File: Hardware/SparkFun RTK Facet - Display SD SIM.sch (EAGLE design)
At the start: 31 parts, among them J1 FPC_12_0.5MM2, J16 microSD, J17 NANO_SIM, J2 FPC_12_0.5MM2, U13 LIS2DH12

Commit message: Update PROD ID on 12 pin connector. Add gerbers for v10.
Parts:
- J1, J2: value FPC_12_0.5MM2 -> FPC_12_0.5MM_BACKFLIP; device RTK Facet:FPC_12_0.5MM2 -> RTK Facet:FPC_12_0.5MM_BACKFLIP
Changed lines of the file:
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@@
 <part name="SUPPLY3" library="SparkFun-PowerSymbols" deviceset="3.3V" device=""/>
 <part name="GND2" library="SparkFun-PowerSymbols" deviceset="GND" device=""/>
-<part name="J1" library="RTK Facet" deviceset="FPC_12_0.5MM" device="2" value="FPC_12_0.5MM2"/>
+<part name="J1" library="RTK Facet" deviceset="FPC_12_0.5MM" device="_BACKFLIP" value="FPC_12_0.5MM_BACKFLIP"/>
 <part name="U13" library="SparkFun-Sensors" deviceset="LIS2DH12" device=""/>
 <part name="GND4" library="SparkFun-PowerSymbols" deviceset="GND" device=""/>
@@
 <part name="J17" library="ublox" deviceset="NANO_SIM" device="WURTH" value="NANO_SIM"/>
 <part name="GND5" library="SparkFun-PowerSymbols" deviceset="GND" device=""/>
-<part name="J2" library="RTK Facet" deviceset="FPC_12_0.5MM" device="2" value="FPC_12_0.5MM2"/>
+<part name="J2" library="RTK Facet" deviceset="FPC_12_0.5MM" device="_BACKFLIP" value="FPC_12_0.5MM_BACKFLIP"/>
 <part name="S1" library="SparkFun-Switches" deviceset="MOMENTARY-SWITCH-SPST" device="-SMD-5.2MM-TALL" value=""/>
 <part name="GND6" library="SparkFun-PowerSymbols" deviceset="GND" device=""/>

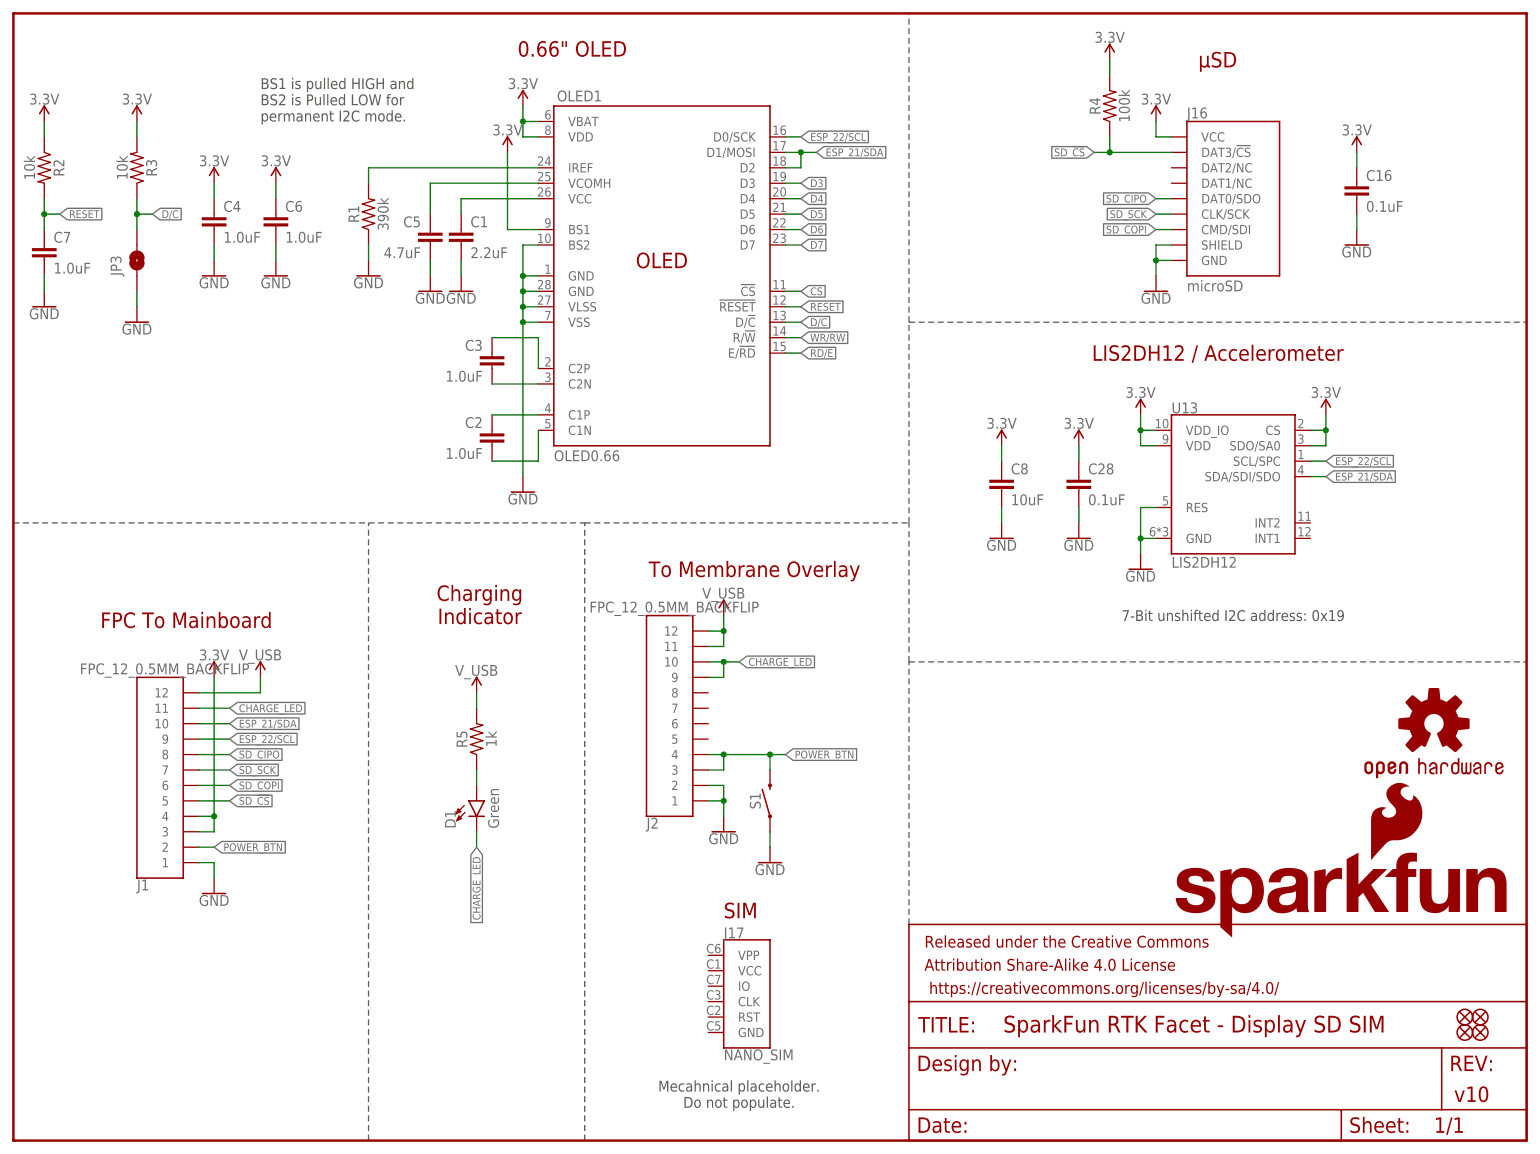
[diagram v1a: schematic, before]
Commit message: Move overlay connector further down. Invert overlay connector pins.
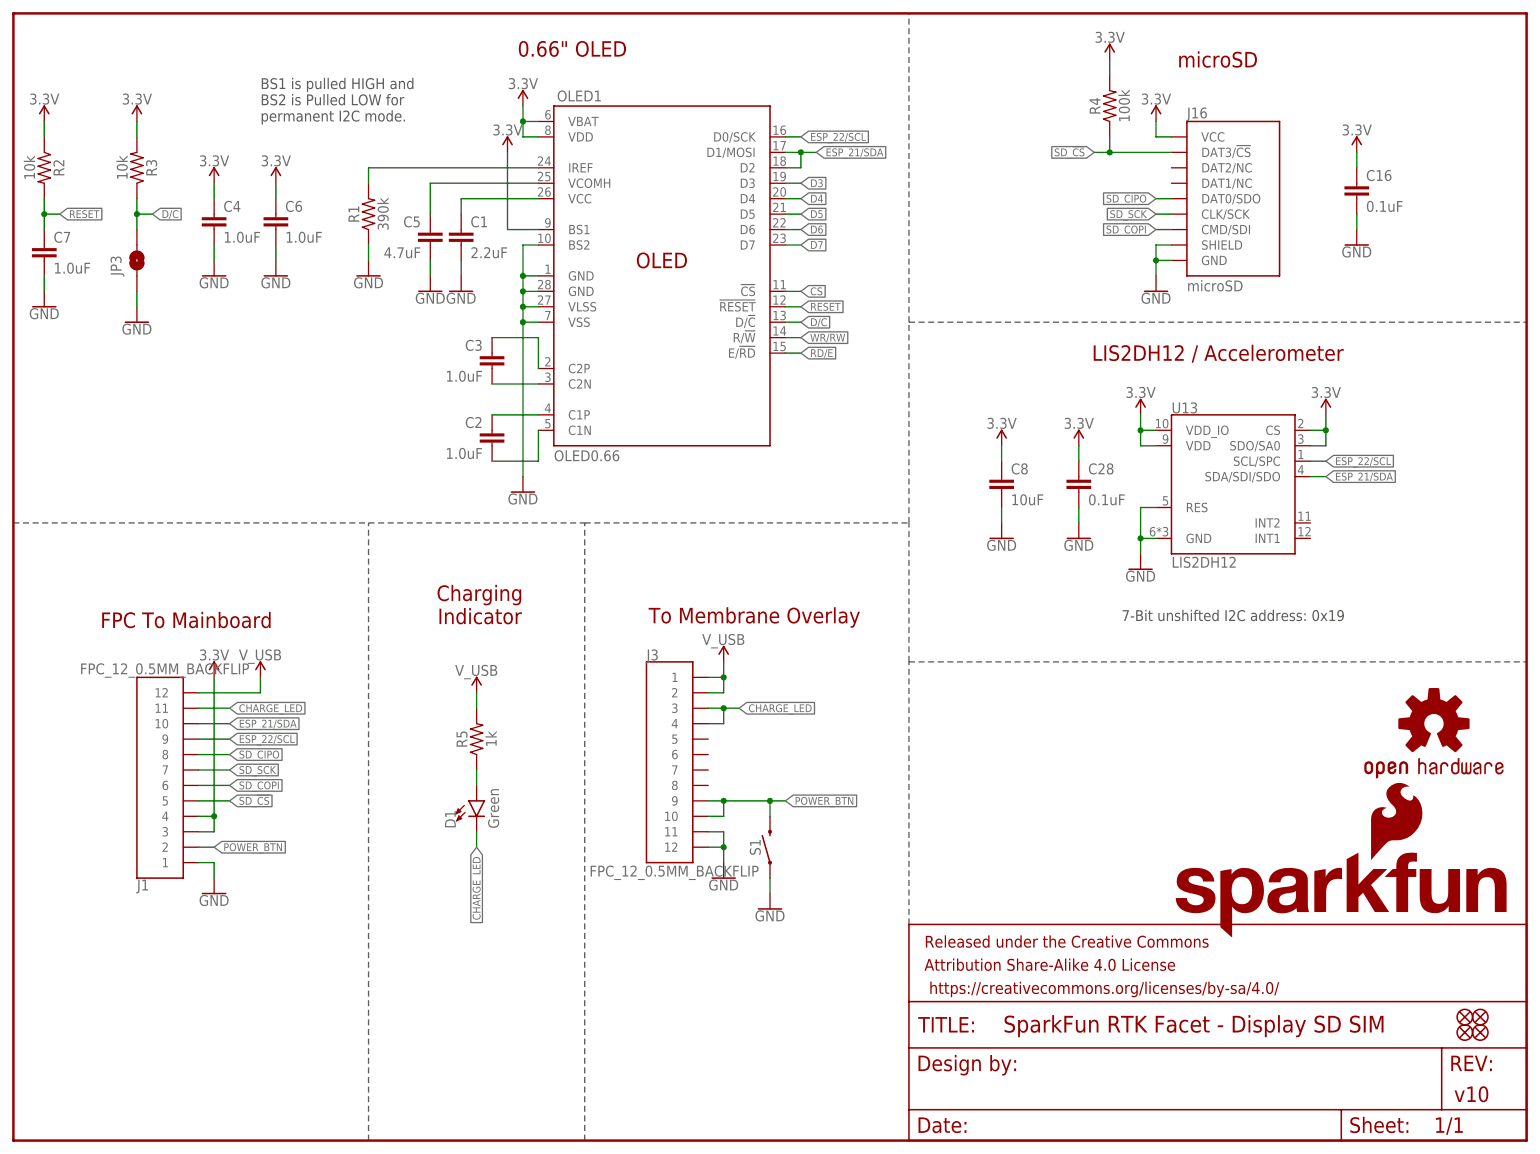
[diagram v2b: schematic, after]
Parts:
- removed J17: NANO_SIM, ublox:NANO_SIMWURTH
- removed J2: FPC_12_0.5MM_BACKFLIP, RTK Facet:FPC_12_0.5MM_BACKFLIP
- added J3: FPC_12_0.5MM_BACKFLIP, RTK Facet:FPC_12_0.5MM_BACKFLIP
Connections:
- net CHARGE_LED: now also J3.3, J3.4; no longer J2.10, J2.9
- net GND: now also J3.11, J3.12; no longer J2.1, J2.2
- net POWER_BTN: now also J3.10, J3.9; no longer J2.3, J2.4
- net V_USB: now also J3.1, J3.2; no longer J2.11, J2.12
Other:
- note added: "microSD"
- note removed: "Mecahnical placeholder. Do not populate."
- note removed: "SIM"
- note removed: "μSD"
- moved on the sheet: S1
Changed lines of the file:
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@@
 <part name="SUPPLY7" library="SparkFun-PowerSymbols" deviceset="3.3V" device=""/>
 <part name="SUPPLY8" library="SparkFun-PowerSymbols" deviceset="3.3V" device=""/>
-<part name="J17" library="ublox" deviceset="NANO_SIM" device="WURTH" value="NANO_SIM"/>
 <part name="GND5" library="SparkFun-PowerSymbols" deviceset="GND" device=""/>
-<part name="J2" library="RTK Facet" deviceset="FPC_12_0.5MM" device="_BACKFLIP" value="FPC_12_0.5MM_BACKFLIP"/>
 <part name="S1" library="SparkFun-Switches" deviceset="MOMENTARY-SWITCH-SPST" device="-SMD-5.2MM-TALL" value=""/>
 <part name="GND6" library="SparkFun-PowerSymbols" deviceset="GND" device=""/>
@@
 <part name="SUPPLY11" library="SparkFun-PowerSymbols" deviceset="V_USB" device=""/>
 <part name="SUPPLY4" library="SparkFun-PowerSymbols" deviceset="V_USB" device=""/>
+<part name="J3" library="RTK Facet" deviceset="FPC_12_0.5MM" device="_BACKFLIP" value="FPC_12_0.5MM_BACKFLIP"/>
 </parts>
 <sheets>
@@
 BS2 is Pulled LOW for
 permanent I2C mode.</text>
-<text x="198.12" y="177.8" size="2.54" layer="94" align="center">μSD</text>
+<text x="198.12" y="177.8" size="2.54" layer="94" align="center">microSD</text>
 <text x="200.66" y="86.36" size="1.778" layer="97" align="center">7-Bit unshifted I2C address: 0x19</text>
 <text x="198.12" y="129.54" size="2.54" layer="94" font="vector" align="center">LIS2DH12 / Accelerometer</text>
-<text x="119.634" y="37.846" size="2.54" layer="94" font="vector" align="center">SIM</text>
-<text x="119.38" y="7.62" size="1.778" layer="97" align="center">Mecahnical placeholder.
-Do not populate.</text>
-<text x="121.92" y="93.98" size="2.54" layer="94" rot="MR180" align="center">To Membrane Overlay</text>
+<text x="121.92" y="86.36" size="2.54" layer="94" rot="MR180" align="center">To Membrane Overlay</text>
 <wire x1="0" y1="101.6" x2="58.42" y2="101.6" width="0.2032" layer="97" style="shortdash"/>
 <text x="91.948" y="179.578" size="2.54" layer="94" align="center">0.66" OLED</text>
@@
 <attribute name="VALUE" x="215.9" y="122.174" size="1.778" layer="96" align="bottom-center"/>
 </instance>
-<instance part="J17" gate="G$1" x="121.92" y="22.86" smashed="yes">
-<attribute name="NAME" x="116.84" y="33.274" size="1.778" layer="95"/>
-<attribute name="VALUE" x="116.84" y="14.986" size="1.778" layer="96" align="top-left"/>
-</instance>
-<instance part="GND5" gate="1" x="116.84" y="50.8" smashed="yes">
-<attribute name="VALUE" x="116.84" y="50.546" size="1.778" layer="96" align="top-center"/>
-</instance>
-<instance part="J2" gate="J1" x="106.68" y="68.58" smashed="yes" rot="MR180">
-<attribute name="NAME" x="104.14" y="53.086" size="1.778" layer="95" rot="MR180"/>
-<attribute name="VALUE" x="94.742" y="88.646" size="1.778" layer="96" rot="MR180"/>
-</instance>
-<instance part="S1" gate="G$1" x="124.46" y="55.88" smashed="yes" rot="R90">
-<attribute name="NAME" x="122.936" y="55.88" size="1.778" layer="95" font="vector" rot="R90" align="bottom-center"/>
-<attribute name="VALUE" x="124.968" y="55.88" size="1.778" layer="96" font="vector" rot="R90" align="top-center"/>
-</instance>
-<instance part="GND6" gate="1" x="124.46" y="45.72" smashed="yes">
-<attribute name="VALUE" x="124.46" y="45.466" size="1.778" layer="96" align="top-center"/>
+<instance part="GND5" gate="1" x="116.84" y="43.18" smashed="yes">
+<attribute name="VALUE" x="116.84" y="42.926" size="1.778" layer="96" align="top-center"/>
+</instance>
+<instance part="S1" gate="G$1" x="124.46" y="48.26" smashed="yes" rot="R90">
+<attribute name="NAME" x="122.936" y="48.26" size="1.778" layer="95" font="vector" rot="R90" align="bottom-center"/>
+<attribute name="VALUE" x="124.968" y="48.26" size="1.778" layer="96" font="vector" rot="R90" align="top-center"/>
+</instance>
+<instance part="GND6" gate="1" x="124.46" y="38.1" smashed="yes">
+<attribute name="VALUE" x="124.46" y="37.846" size="1.778" layer="96" align="top-center"/>
 </instance>
 <instance part="SUPPLY10" gate="G$1" x="40.64" y="76.2" smashed="yes">
@@
 <attribute name="VALUE" x="76.2" y="76.454" size="1.778" layer="96" align="bottom-center"/>
 </instance>
-<instance part="SUPPLY4" gate="G$1" x="116.84" y="86.36" smashed="yes">
-<attribute name="VALUE" x="116.84" y="89.154" size="1.778" layer="96" align="bottom-center"/>
+<instance part="SUPPLY4" gate="G$1" x="116.84" y="78.74" smashed="yes">
+<attribute name="VALUE" x="116.84" y="81.534" size="1.778" layer="96" align="bottom-center"/>
+</instance>
+<instance part="J3" gate="J1" x="106.68" y="63.5" smashed="yes">
+<attribute name="NAME" x="104.14" y="78.994" size="1.778" layer="95"/>
+<attribute name="VALUE" x="94.742" y="43.434" size="1.778" layer="96"/>
 </instance>
 </instances>
@@
 </segment>
 <segment>
-<wire x1="114.3" y1="55.88" x2="116.84" y2="55.88" width="0.1524" layer="91"/>
-<wire x1="116.84" y1="55.88" x2="116.84" y2="53.34" width="0.1524" layer="91"/>
+<wire x1="114.3" y1="48.26" x2="116.84" y2="48.26" width="0.1524" layer="91"/>
+<wire x1="116.84" y1="48.26" x2="116.84" y2="45.72" width="0.1524" layer="91"/>
 <pinref part="GND5" gate="1" pin="GND"/>
-<pinref part="J2" gate="J1" pin="1"/>
-<pinref part="J2" gate="J1" pin="2"/>
-<wire x1="114.3" y1="58.42" x2="116.84" y2="58.42" width="0.1524" layer="91"/>
-<wire x1="116.84" y1="58.42" x2="116.84" y2="55.88" width="0.1524" layer="91"/>
-<junction x="116.84" y="55.88"/>
+<wire x1="114.3" y1="50.8" x2="116.84" y2="50.8" width="0.1524" layer="91"/>
+<wire x1="116.84" y1="50.8" x2="116.84" y2="48.26" width="0.1524" layer="91"/>
+<junction x="116.84" y="48.26"/>
+<pinref part="J3" gate="J1" pin="11"/>
+<pinref part="J3" gate="J1" pin="12"/>
 </segment>
 <segment>
 <pinref part="S1" gate="G$1" pin="1"/>
 <pinref part="GND6" gate="1" pin="GND"/>
-<wire x1="124.46" y1="48.26" x2="124.46" y2="50.8" width="0.1524" layer="91"/>
+<wire x1="124.46" y1="40.64" x2="124.46" y2="43.18" width="0.1524" layer="91"/>
 </segment>
 </net>
@@
 </segment>
 <segment>
-<wire x1="114.3" y1="78.74" x2="116.84" y2="78.74" width="0.1524" layer="91"/>
-<label x="119.38" y="78.74" size="1.27" layer="95" xref="yes"/>
-<pinref part="J2" gate="J1" pin="10"/>
-<pinref part="J2" gate="J1" pin="9"/>
-<wire x1="116.84" y1="78.74" x2="119.38" y2="78.74" width="0.1524" layer="91"/>
-<wire x1="114.3" y1="76.2" x2="116.84" y2="76.2" width="0.1524" layer="91"/>
-<wire x1="116.84" y1="76.2" x2="116.84" y2="78.74" width="0.1524" layer="91"/>
-<junction x="116.84" y="78.74"/>
+<wire x1="114.3" y1="71.12" x2="116.84" y2="71.12" width="0.1524" layer="91"/>
+<label x="119.38" y="71.12" size="1.27" layer="95" xref="yes"/>
+<wire x1="116.84" y1="71.12" x2="119.38" y2="71.12" width="0.1524" layer="91"/>
+<wire x1="114.3" y1="68.58" x2="116.84" y2="68.58" width="0.1524" layer="91"/>
+<wire x1="116.84" y1="68.58" x2="116.84" y2="71.12" width="0.1524" layer="91"/>
+<junction x="116.84" y="71.12"/>
+<pinref part="J3" gate="J1" pin="3"/>
+<pinref part="J3" gate="J1" pin="4"/>
 </segment>
 </net>
@@
 <net name="POWER_BTN" class="0">
 <segment>
-<wire x1="114.3" y1="63.5" x2="116.84" y2="63.5" width="0.1524" layer="91"/>
-<label x="127" y="63.5" size="1.27" layer="95" xref="yes"/>
-<pinref part="J2" gate="J1" pin="4"/>
-<pinref part="J2" gate="J1" pin="3"/>
-<wire x1="116.84" y1="63.5" x2="124.46" y2="63.5" width="0.1524" layer="91"/>
-<wire x1="124.46" y1="63.5" x2="127" y2="63.5" width="0.1524" layer="91"/>
-<wire x1="114.3" y1="60.96" x2="116.84" y2="60.96" width="0.1524" layer="91"/>
-<wire x1="116.84" y1="60.96" x2="116.84" y2="63.5" width="0.1524" layer="91"/>
-<junction x="116.84" y="63.5"/>
+<wire x1="114.3" y1="55.88" x2="116.84" y2="55.88" width="0.1524" layer="91"/>
+<label x="127" y="55.88" size="1.27" layer="95" xref="yes"/>
+<wire x1="116.84" y1="55.88" x2="124.46" y2="55.88" width="0.1524" layer="91"/>
+<wire x1="124.46" y1="55.88" x2="127" y2="55.88" width="0.1524" layer="91"/>
+<wire x1="114.3" y1="53.34" x2="116.84" y2="53.34" width="0.1524" layer="91"/>
+<wire x1="116.84" y1="53.34" x2="116.84" y2="55.88" width="0.1524" layer="91"/>
+<junction x="116.84" y="55.88"/>
 <pinref part="S1" gate="G$1" pin="2"/>
-<wire x1="124.46" y1="60.96" x2="124.46" y2="63.5" width="0.1524" layer="91"/>
-<junction x="124.46" y="63.5"/>
+<wire x1="124.46" y1="53.34" x2="124.46" y2="55.88" width="0.1524" layer="91"/>
+<junction x="124.46" y="55.88"/>
+<pinref part="J3" gate="J1" pin="9"/>
+<pinref part="J3" gate="J1" pin="10"/>
 </segment>
 <segment>
@@
 </segment>
 <segment>
-<wire x1="114.3" y1="83.82" x2="116.84" y2="83.82" width="0.1524" layer="91"/>
-<wire x1="116.84" y1="83.82" x2="116.84" y2="86.36" width="0.1524" layer="91"/>
-<pinref part="J2" gate="J1" pin="12"/>
-<pinref part="J2" gate="J1" pin="11"/>
-<wire x1="114.3" y1="81.28" x2="116.84" y2="81.28" width="0.1524" layer="91"/>
-<wire x1="116.84" y1="81.28" x2="116.84" y2="83.82" width="0.1524" layer="91"/>
-<junction x="116.84" y="83.82"/>
+<wire x1="114.3" y1="76.2" x2="116.84" y2="76.2" width="0.1524" layer="91"/>
+<wire x1="116.84" y1="76.2" x2="116.84" y2="78.74" width="0.1524" layer="91"/>
+<wire x1="114.3" y1="73.66" x2="116.84" y2="73.66" width="0.1524" layer="91"/>
+<wire x1="116.84" y1="73.66" x2="116.84" y2="76.2" width="0.1524" layer="91"/>
+<junction x="116.84" y="76.2"/>
 <pinref part="SUPPLY4" gate="G$1" pin="V_USB"/>
-</segment>
-</net>
+<pinref part="J3" gate="J1" pin="1"/>
+<pinref part="J3" gate="J1" pin="2"/>
+</segment>
+</net>
